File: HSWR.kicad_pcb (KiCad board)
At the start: 4 copper layers, 152 x 139 mm, 167 parts, among them IC1 B1212S-2W, IC2 JW5052C, IC3 JW5052C, IC4 ADUM3054, IC5 ADuM4160, J1 USB_B, J2 IO, J3 B+, J4 B-, J5 U, J6 V, J7 W, J8 SWD, J9 AVR-ISP-6, Q1 IXFK300N20X3, Q2 IXFK300N20X3, Q3 IXFK300N20X3, Q4 IXFK300N20X3, Q5 IXFK300N20X3, Q6 IXFK300N20X3, Q7 Q_NMOS_GDS, U1 ACS781xLRTR-150B, U10 AM26LV32xD, U11 ADuM120N, U12 ADuM120N, U13 PC355, U2 ACS781xLRTR-150B, U3 ACS781xLRTR-150B, U4 STM32F405RGTx, U5 IRS2186, U6 IRS2186, U7 IRS2186, U8 AP1117-50, U9 ATtiny13A-SU, Y1 8MHz

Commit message: - renamed ADUM3054 as ADM3054 - specified ADuM120N1 (fail high)
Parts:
- IC4: value ADUM3054 -> ADM3054
- U11, U12: value ADuM120N -> ADuM120N1
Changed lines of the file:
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@@
     (add_net "Net-(IC3-Pad3)")
     (add_net "Net-(IC3-Pad4)")
+    (add_net "Net-(IC4-Pad10)")
     (add_net "Net-(IC5-Pad10)")
     (add_net "Net-(IC5-Pad11)")
     (add_net "Net-(IC5-Pad6)")
     (add_net "Net-(IC5-Pad7)")
+    (add_net "Net-(J8-Pad6)")
     (add_net "Net-(J9-Pad1)")
     (add_net "Net-(J9-Pad3)")
@@
     (add_net "Net-(R26-Pad2)")
     (add_net "Net-(R37-Pad2)")
+    (add_net "Net-(U1-Pad4)")
+    (add_net "Net-(U1-Pad7)")
+    (add_net "Net-(U10-Pad4)")
+    (add_net "Net-(U2-Pad4)")
+    (add_net "Net-(U2-Pad7)")
+    (add_net "Net-(U3-Pad4)")
+    (add_net "Net-(U3-Pad7)")
+    (add_net "Net-(U4-Pad2)")
+    (add_net "Net-(U4-Pad20)")
+    (add_net "Net-(U4-Pad21)")
+    (add_net "Net-(U4-Pad22)")
+    (add_net "Net-(U4-Pad23)")
+    (add_net "Net-(U4-Pad24)")
+    (add_net "Net-(U4-Pad25)")
+    (add_net "Net-(U4-Pad26)")
+    (add_net "Net-(U4-Pad27)")
+    (add_net "Net-(U4-Pad28)")
+    (add_net "Net-(U4-Pad3)")
+    (add_net "Net-(U4-Pad33)")
+    (add_net "Net-(U4-Pad4)")
+    (add_net "Net-(U4-Pad40)")
+    (add_net "Net-(U4-Pad53)")
+    (add_net "Net-(U4-Pad54)")
+    (add_net "Net-(U4-Pad55)")
+    (add_net "Net-(U4-Pad56)")
+    (add_net "Net-(U4-Pad57)")
+    (add_net "Net-(U4-Pad58)")
+    (add_net "Net-(U4-Pad59)")
     (add_net SWCLK)
     (add_net SWDIO)
@@
       (effects (font (size 1 1) (thickness 0.15)))
     )
-    (fp_text value ADuM120N (at 0 3.4) (layer F.Fab)
+    (fp_text value ADuM120N1 (at 0 3.4) (layer F.Fab)
       (effects (font (size 1 1) (thickness 0.15)))
     )
@@
       (effects (font (size 1 1) (thickness 0.15)))
     )
-    (fp_text value ADuM120N (at 0 3.4) (layer F.Fab)
+    (fp_text value ADuM120N1 (at 0 3.4) (layer F.Fab)
       (effects (font (size 1 1) (thickness 0.15)))
     )
@@
       (effects (font (size 1 1) (thickness 0.15)))
     )
-    (fp_text value ADUM3054 (at 0 6.25 180) (layer F.Fab)
+    (fp_text value ADM3054 (at 0 6.25 180) (layer F.Fab)
       (effects (font (size 1 1) (thickness 0.15)))
     )

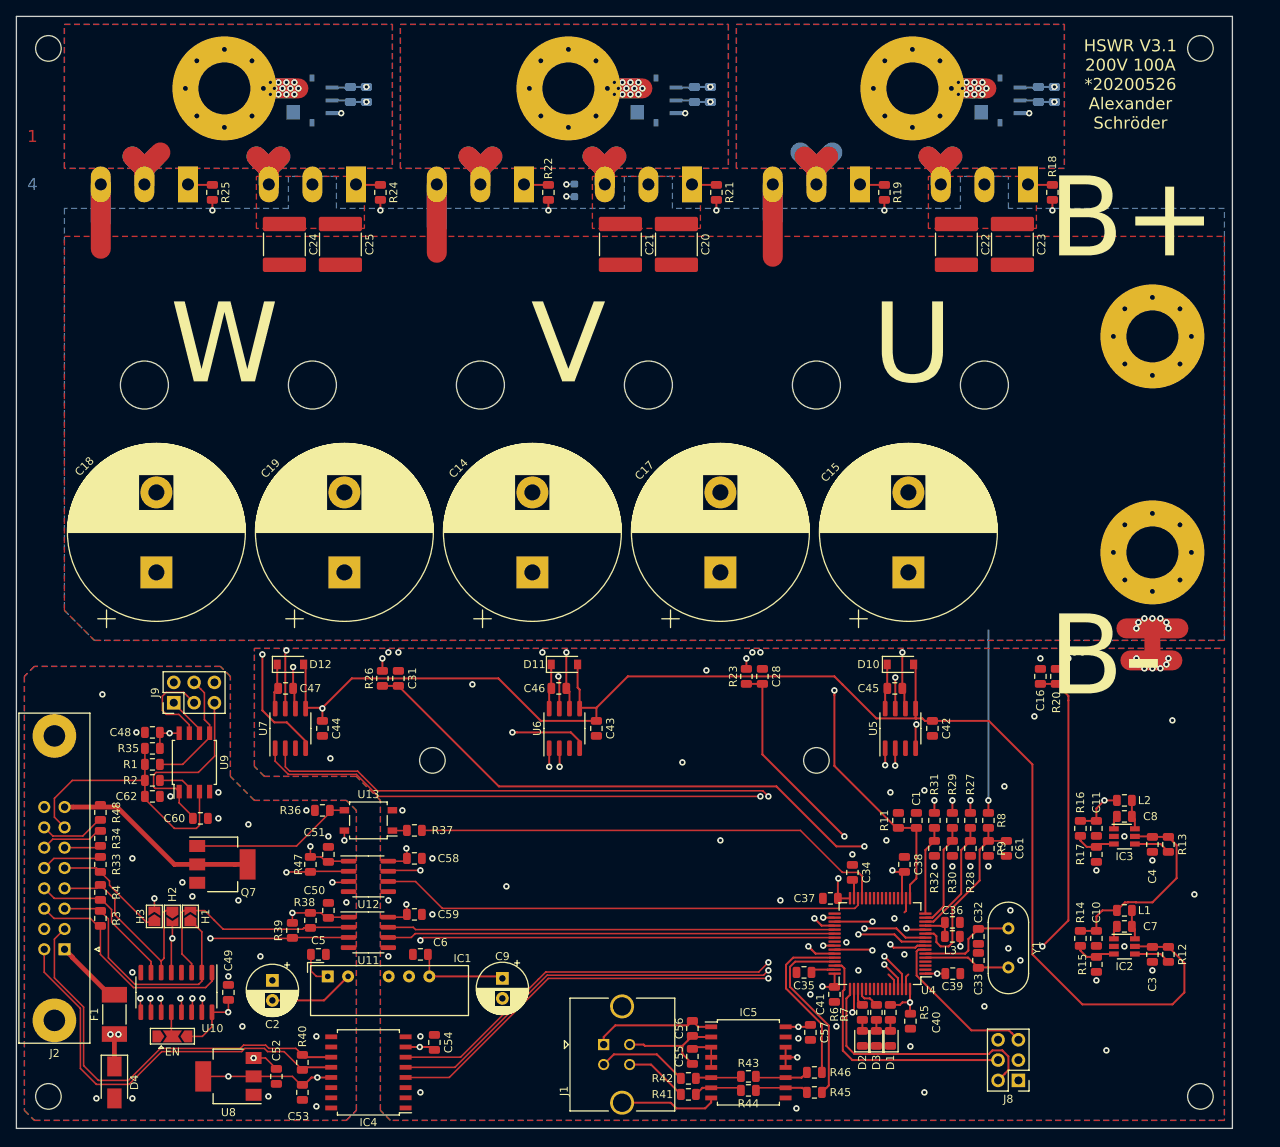
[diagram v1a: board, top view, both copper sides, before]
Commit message: - added fiducials - updated silkscreen - removed ghost traces - optimized top layer polygons - increased insulation distance on HV nets - added vias around current sensor to make use of inner layers
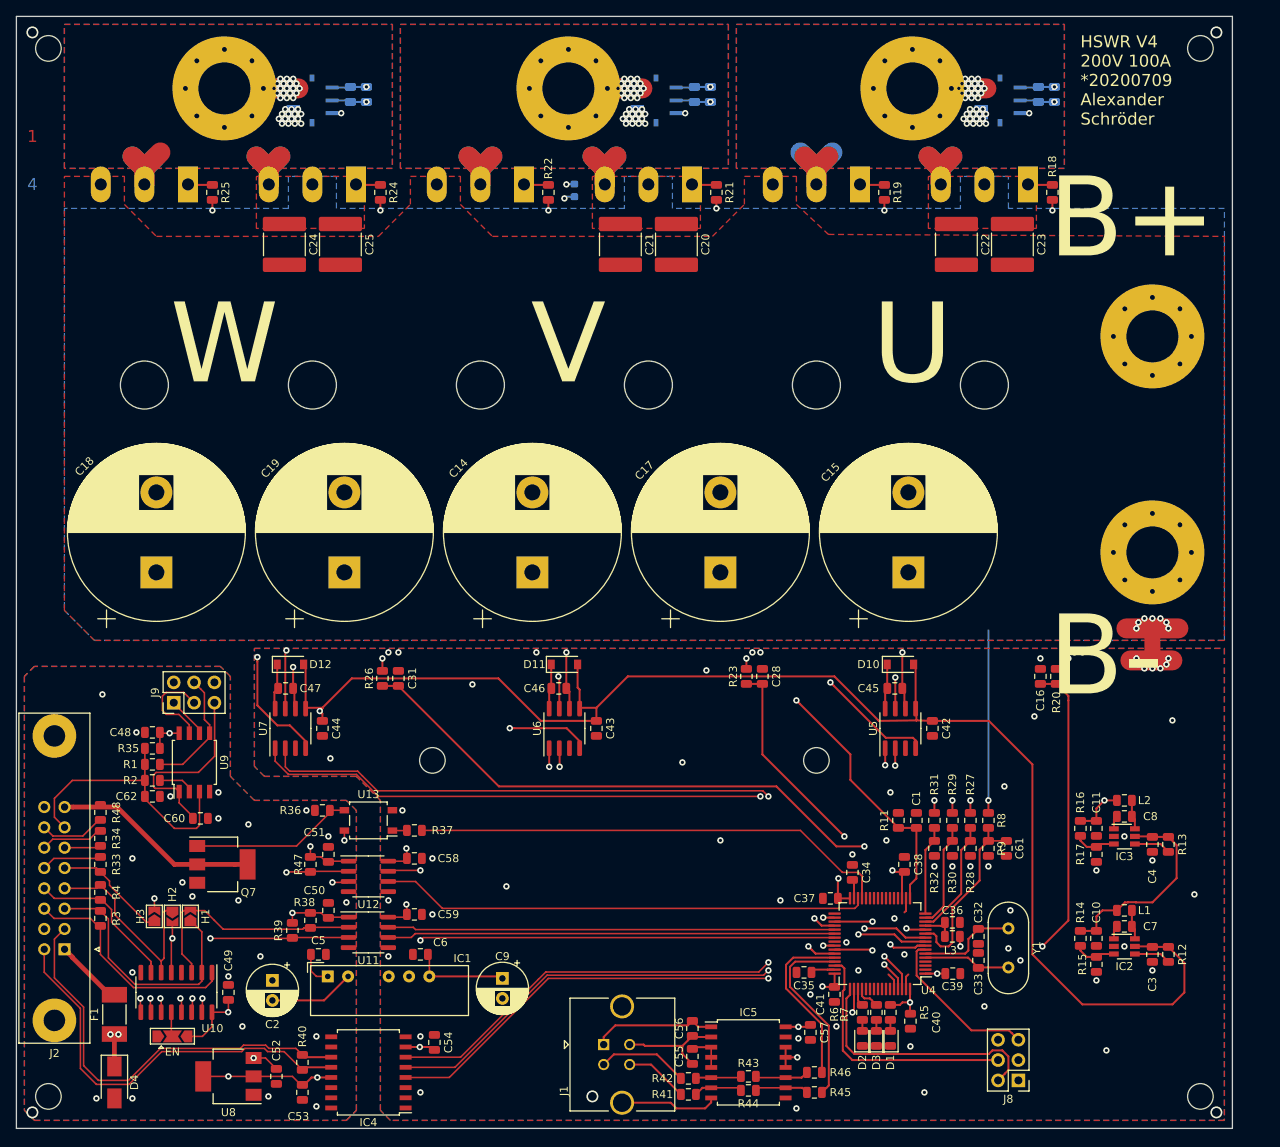
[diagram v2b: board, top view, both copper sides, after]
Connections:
- IC4 pad 10: (no net) -> Net-(IC4-Pad10)
- J8 pad 6: (no net) -> Net-(J8-Pad6)
- U1 pad 4: (no net) -> Net-(U1-Pad4)
- U1 pad 7: (no net) -> Net-(U1-Pad7)
- U10 pad 4: (no net) -> Net-(U10-Pad4)
- U2 pad 4: (no net) -> Net-(U2-Pad4)
- U2 pad 7: (no net) -> Net-(U2-Pad7)
- U3 pad 4: (no net) -> Net-(U3-Pad4)
- U3 pad 7: (no net) -> Net-(U3-Pad7)
- U4 pad 2: (no net) -> Net-(U4-Pad2)
- U4 pad 20: (no net) -> Net-(U4-Pad20)
- U4 pad 21: (no net) -> Net-(U4-Pad21)
- U4 pad 22: (no net) -> Net-(U4-Pad22)
- U4 pad 23: (no net) -> Net-(U4-Pad23)
- U4 pad 24: (no net) -> Net-(U4-Pad24)
- U4 pad 25: (no net) -> Net-(U4-Pad25)
- U4 pad 26: (no net) -> Net-(U4-Pad26)
- U4 pad 27: (no net) -> Net-(U4-Pad27)
- U4 pad 28: (no net) -> Net-(U4-Pad28)
- U4 pad 3: (no net) -> Net-(U4-Pad3)
- U4 pad 33: (no net) -> Net-(U4-Pad33)
- U4 pad 4: (no net) -> Net-(U4-Pad4)
- U4 pad 40: (no net) -> Net-(U4-Pad40)
- U4 pad 53: (no net) -> Net-(U4-Pad53)
- U4 pad 54: (no net) -> Net-(U4-Pad54)
- U4 pad 55: (no net) -> Net-(U4-Pad55)
- U4 pad 56: (no net) -> Net-(U4-Pad56)
- U4 pad 57: (no net) -> Net-(U4-Pad57)
- U4 pad 58: (no net) -> Net-(U4-Pad58)
- U4 pad 59: (no net) -> Net-(U4-Pad59)
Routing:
- net GNDPWR: track 46.6 -> 6.50 mm
- net /Power MOSFETS/U: track 36.3 -> 43.8 mm, vias 12 -> 19
- net /Mosfet driver/U_GL: track 70.3 -> 77.7 mm
- net Net-(R23-Pad2): track 76.6 -> 73.8 mm
- net /MCU/TEMP_INT: track 131.7 -> 130.3 mm
- net /Mosfet driver/W_VP: track 190.2 -> 191.6 mm, vias 2 -> 17
- net +12V: track 232.0 -> 233.3 mm
- net GND: track 241.9 -> 240.8 mm, vias 62 -> 61
- net +3V3: track 343.0 -> 342.0 mm
- net /MCU/V_PWM_L: track 76.7 -> 76.0 mm
- net /MCU/V_PWM_H: track 82.9 -> 82.2 mm
- net /Mosfet driver/U_VP: track 123.0 -> 123.5 mm, vias 2 -> 17
- net /Mosfet driver/V_GL: track 78.3 -> 78.8 mm
- net /Mosfet driver/V_VP: track 162.0 -> 162.2 mm, vias 2 -> 17
- net /Power MOSFETS/W: vias 12 -> 19
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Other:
- net class iso added: clearance 1, trace_width 0.25, via_dia 0.8, via_drill 0.4
- board text added: "HSWR V4 200V 100A *20200709 Alexander Schröder"
- board text removed: "HSWR V3.1 200V 100A *20200526 Alexander Schröder"

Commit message: - last finishing touches - export check - updated README.md
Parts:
- moved C29 2.50 mm to (110.8, 32.2)
- moved C30 2.50 mm to (112.8, 32.2)
- moved J7 2.50 mm to (95.0, 31.5)
- moved U3 2.50 mm to (106.0, 33.0)
- moved C26 1.80 mm to (152.8, 32.2)
- moved C27 1.80 mm to (154.8, 32.2)
- moved J6 1.80 mm to (137.0, 31.5)
- moved U2 1.80 mm to (148.0, 33.0)
- moved C12 1.50 mm to (194.8, 32.2)
- moved C13 1.50 mm to (196.8, 32.2)
- moved J5 1.50 mm to (179.0, 31.5)
- moved U1 1.50 mm to (190.0, 33.0)
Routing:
- net Earth: track 10.7 -> 0.00 mm, vias 22 -> 23
- net GND: track 240.8 -> 242.9 mm
- net Net-(R20-Pad2): track 75.9 -> 77.4 mm
- net +3V3: track 342.0 -> 343.2 mm
- net Net-(R23-Pad2): track 73.8 -> 74.9 mm
- net Net-(R26-Pad2): track 77.1 -> 76.6 mm
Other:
- board text added: "GND Fan- Fan+ MT UB UA H3B H3A H2B H2A H1B H1A GND CanL CanH VCC"
- board text added: "HSWR V4 200V 100A *20200713 Alexander Schröder"
- board text removed: "HSWR V4 200V 100A *20200709 Alexander Schröder"

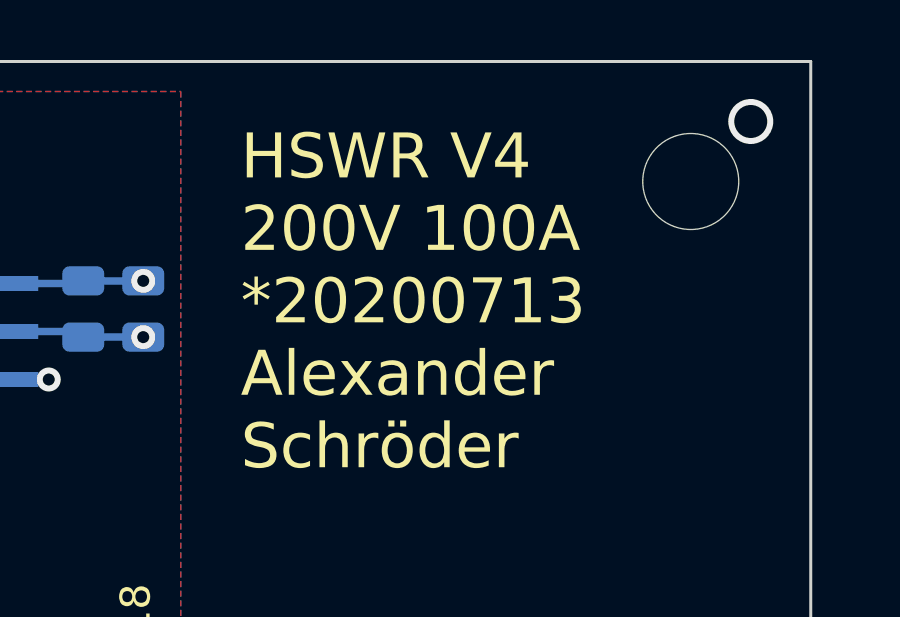
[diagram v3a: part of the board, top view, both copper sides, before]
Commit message: - updated schematic symbols - updated silk screen version label
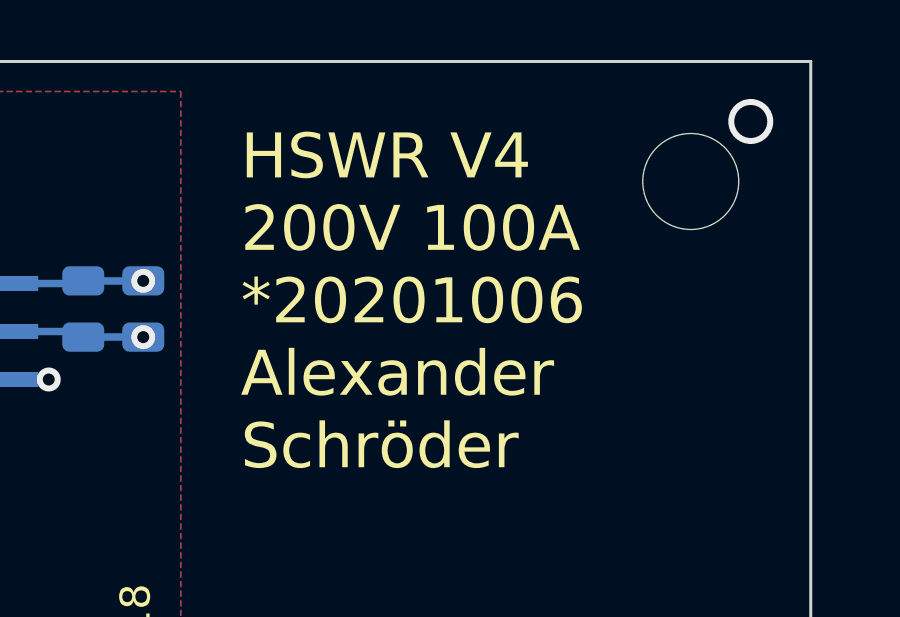
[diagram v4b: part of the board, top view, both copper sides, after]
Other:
- board text added: "HSWR V4 200V 100A *20201006 Alexander Schröder"
- board text removed: "HSWR V4 200V 100A *20200713 Alexander Schröder"
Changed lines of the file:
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@@
     (effects (font (size 10 10) (thickness 1)))
   )
-  (gr_text "HSWR V4\n200V 100A\n*20200713\nAlexander\nSchröder" (at 200 32) (layer F.SilkS)
+  (gr_text "HSWR V4\n200V 100A\n*20201006\nAlexander\nSchröder" (at 200 32) (layer F.SilkS)
     (effects (font (size 1.5 1.5) (thickness 0.3)) (justify left))
   )

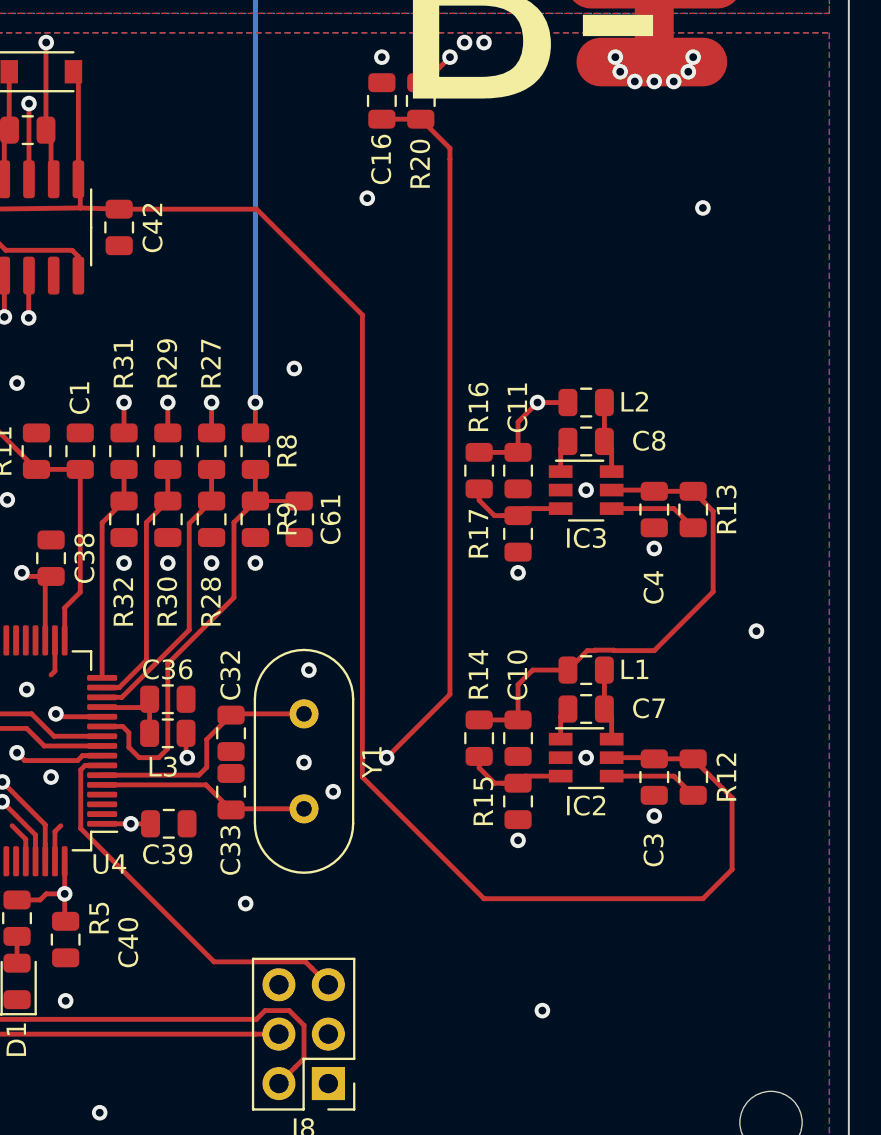
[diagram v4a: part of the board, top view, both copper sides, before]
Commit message: - removed 5V DCDC because unused
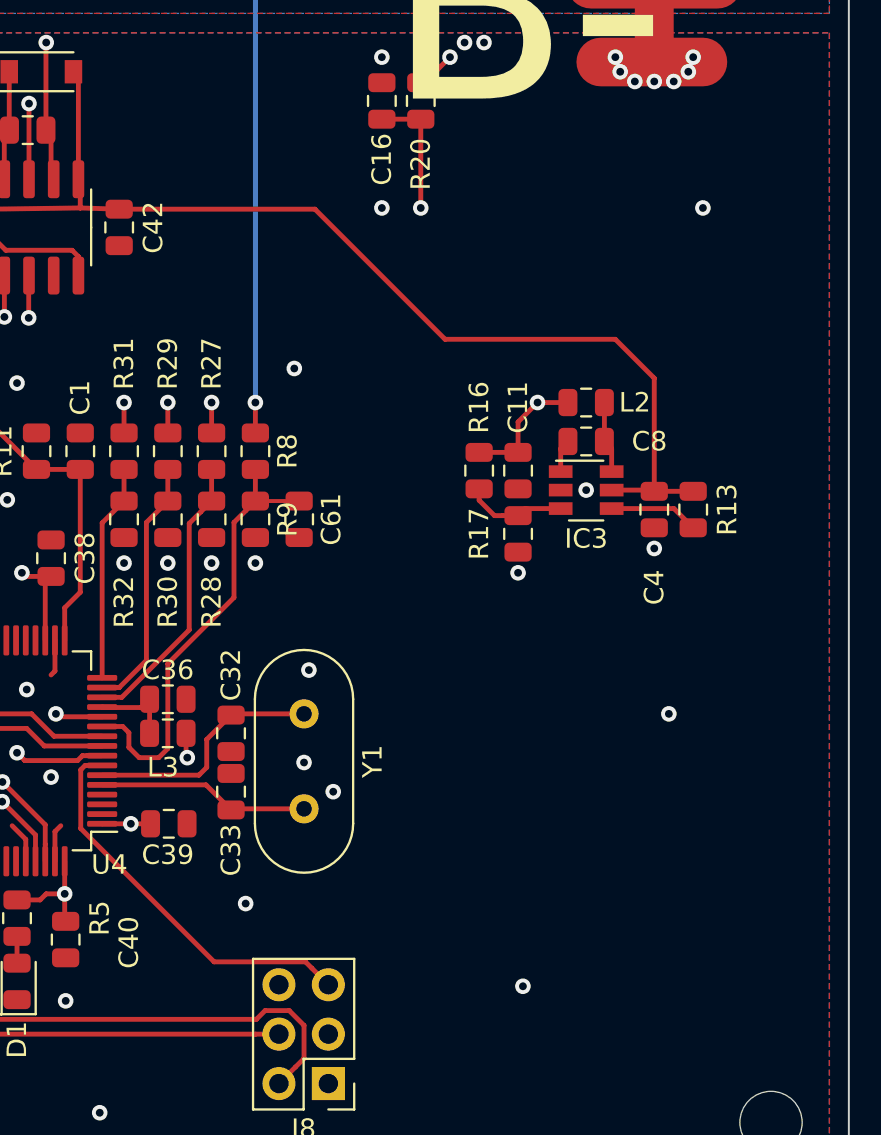
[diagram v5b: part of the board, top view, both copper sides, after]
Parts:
- removed C10: 22u/6V3, Capacitor_SMD:C_0805_2012Metric
- removed C3: 22u/16V, Capacitor_SMD:C_0805_2012Metric
- removed C7: 100n, Capacitor_SMD:C_0805_2012Metric
- removed IC2: JW5052C, Package_TO_SOT_SMD:TSOT-23-6
- removed L1: FCI201209F-4R7K, Inductor_SMD:L_0805_2012Metric
- removed R12: 100k, Resistor_SMD:R_0805_2012Metric
- removed R14: 110k, Resistor_SMD:R_0805_2012Metric
- removed R15: 15k, Resistor_SMD:R_0805_2012Metric
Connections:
- C4 pad 1: +5V -> +12V
- IC3 pad 5: +5V -> +12V
- IC4 pad 10: Net-(IC4-Pad10) -> (no net)
- J8 pad 6: Net-(J8-Pad6) -> (no net)
- R13 pad 2: +5V -> +12V
- U1 pad 4: Net-(U1-Pad4) -> (no net)
- U1 pad 7: Net-(U1-Pad7) -> (no net)
- U10 pad 4: Net-(U10-Pad4) -> (no net)
- U2 pad 4: Net-(U2-Pad4) -> (no net)
- U2 pad 7: Net-(U2-Pad7) -> (no net)
- U3 pad 4: Net-(U3-Pad4) -> (no net)
- U3 pad 7: Net-(U3-Pad7) -> (no net)
- U4 pad 2: Net-(U4-Pad2) -> (no net)
- U4 pad 20: Net-(U4-Pad20) -> (no net)
- U4 pad 21: Net-(U4-Pad21) -> (no net)
- U4 pad 22: Net-(U4-Pad22) -> (no net)
- U4 pad 23: Net-(U4-Pad23) -> (no net)
- U4 pad 24: Net-(U4-Pad24) -> (no net)
- U4 pad 25: Net-(U4-Pad25) -> (no net)
- U4 pad 26: Net-(U4-Pad26) -> (no net)
- U4 pad 27: Net-(U4-Pad27) -> (no net)
- U4 pad 28: Net-(U4-Pad28) -> (no net)
- U4 pad 3: Net-(U4-Pad3) -> (no net)
- U4 pad 33: Net-(U4-Pad33) -> (no net)
- U4 pad 4: Net-(U4-Pad4) -> (no net)
- U4 pad 40: Net-(U4-Pad40) -> (no net)
- U4 pad 53: Net-(U4-Pad53) -> (no net)
- U4 pad 54: Net-(U4-Pad54) -> (no net)
- U4 pad 55: Net-(U4-Pad55) -> (no net)
- U4 pad 56: Net-(U4-Pad56) -> (no net)
- U4 pad 57: Net-(U4-Pad57) -> (no net)
- U4 pad 58: Net-(U4-Pad58) -> (no net)
- U4 pad 59: Net-(U4-Pad59) -> (no net)
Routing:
- net +12V: track 233.3 -> 203.0 mm
- net +5V: track 25.6 -> 0.00 mm
- net /MCU/U_I: track 60.9 -> 51.9 mm
- net Net-(IC2-Pad3): track 5.25 -> 0.00 mm
- net Net-(IC2-Pad4): track 4.60 -> 0.00 mm
- net Net-(C7-Pad2): track 3.70 -> 0.00 mm
- net Net-(C7-Pad1): track 1.70 -> 0.00 mm
- net GND: vias 61 -> 58
